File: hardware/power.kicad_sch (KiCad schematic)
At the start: 80 parts, among them Q1 BSN20, Q2 AO3415A, U3 SY8088, U4 SY8088, U5 SY8088, U6 SY8089A, U7 SY8113, U8 SY8088

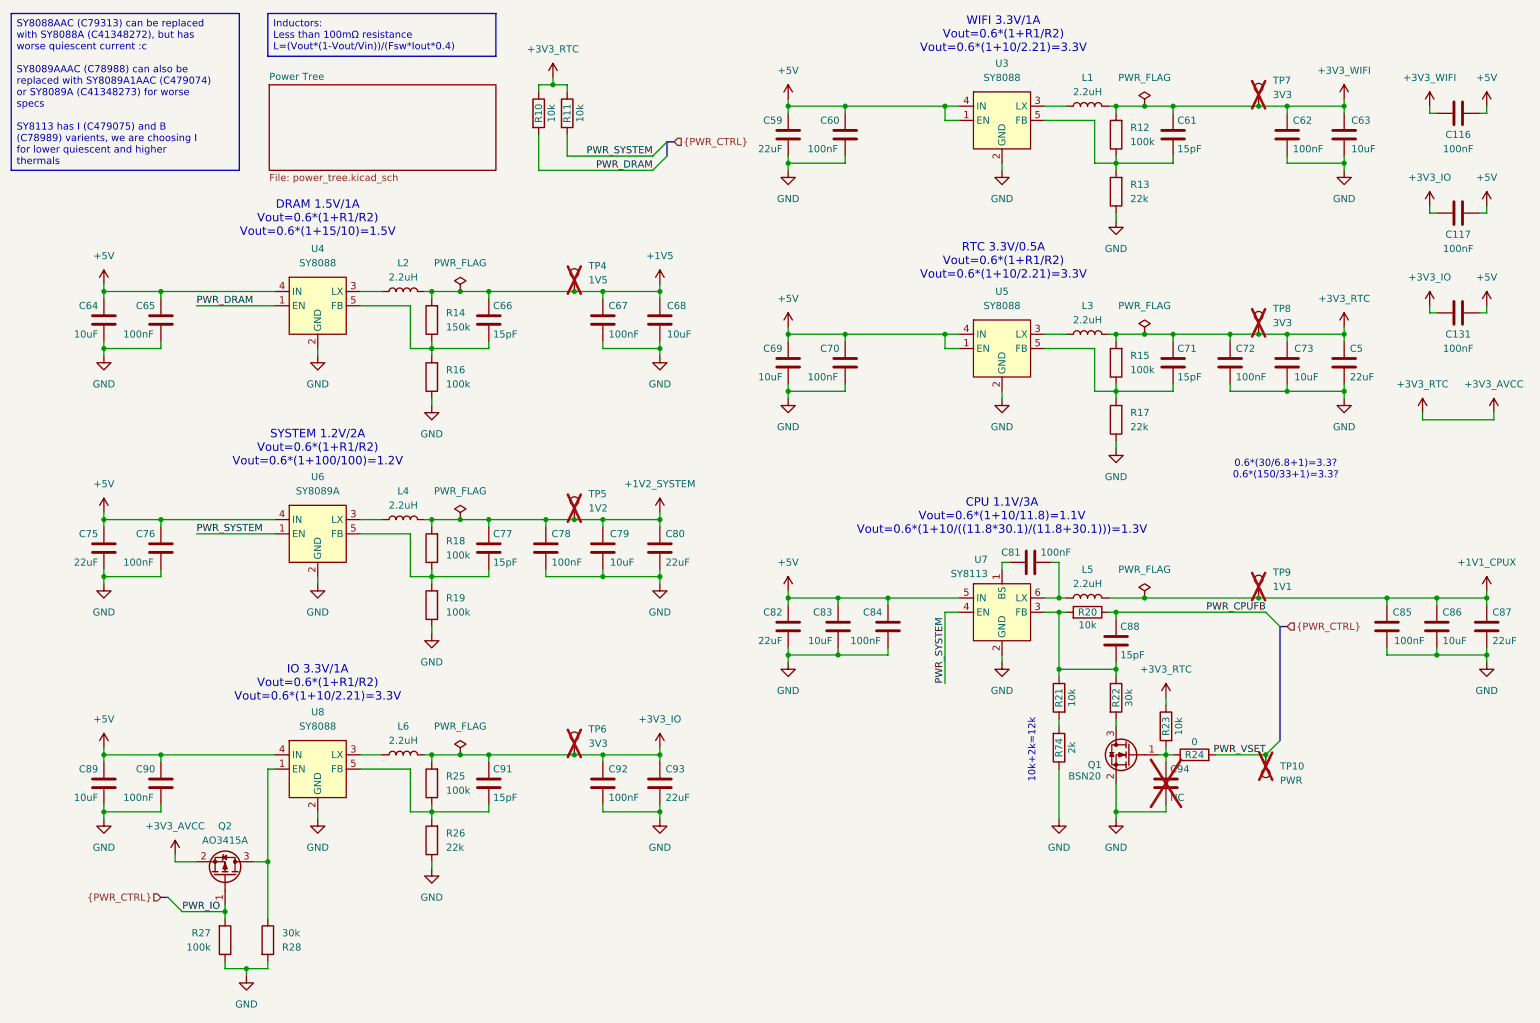
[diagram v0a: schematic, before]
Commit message: Update crystal
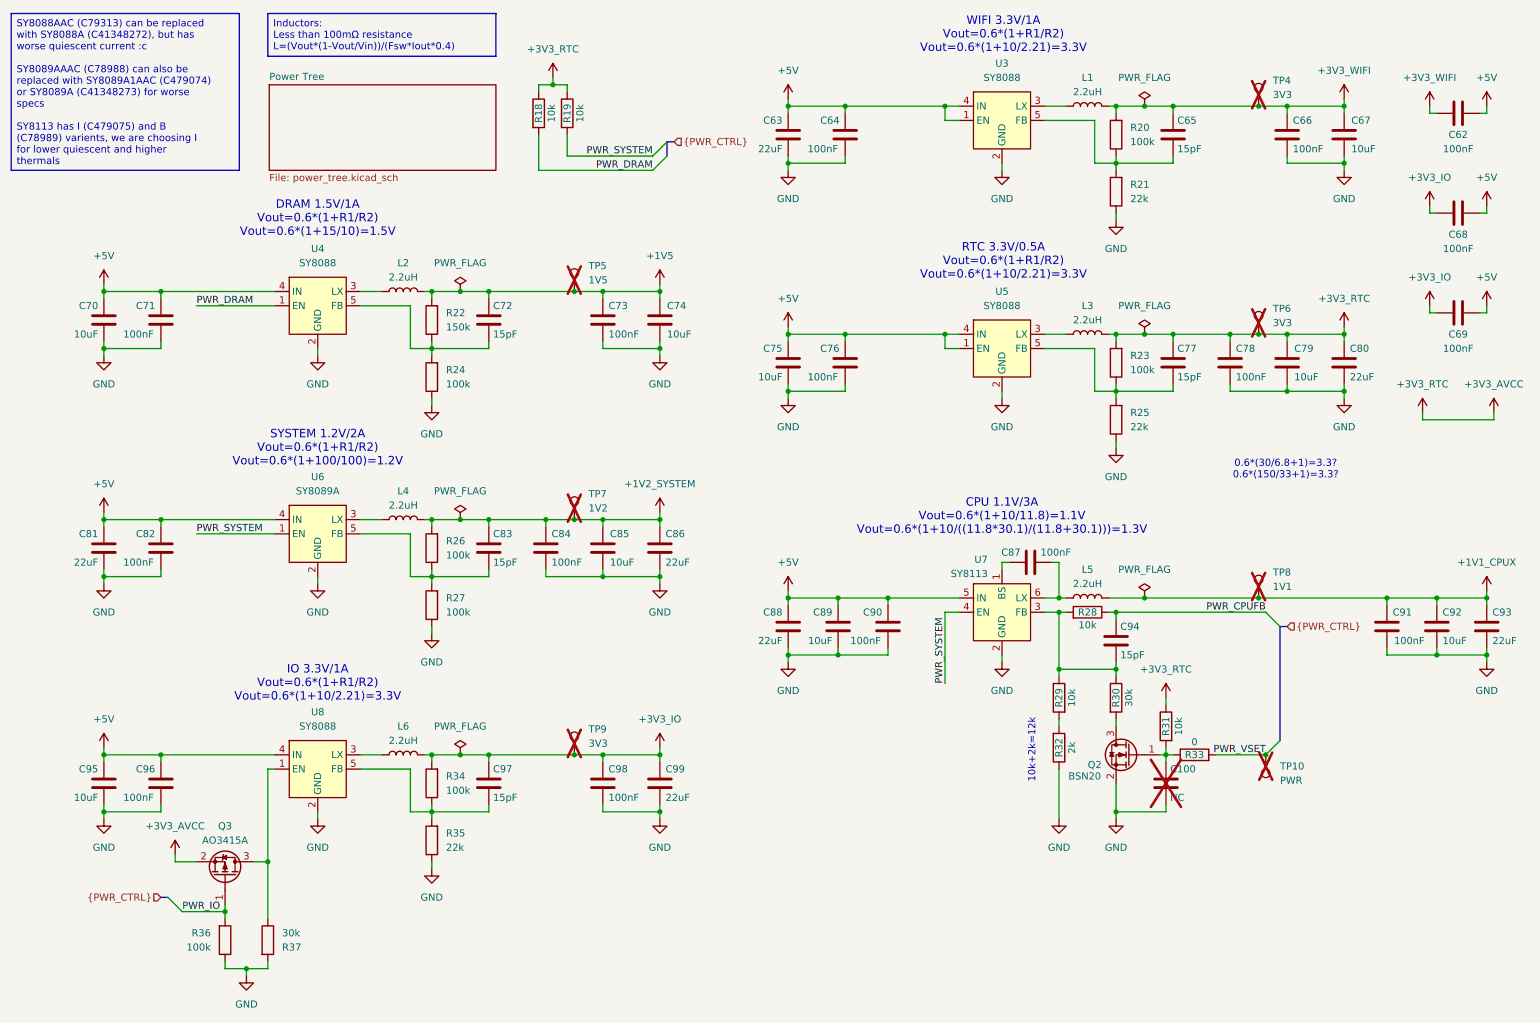
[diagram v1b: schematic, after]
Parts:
- renumbered C94 to C100, C116 to C62, C59 to C63, C60 to C64, C61 to C65, C62 to C66, C63 to C67, C117 to C68, C131 to C69, C64 to C70, C65 to C71, C66 to C72, C67 to C73, C68 to C74, C69 to C75, C70 to C76, C71 to C77, C72 to C78, C73 to C79, C5 to C80, C75 to C81, C76 to C82, C77 to C83, C78 to C84, C79 to C85, C80 to C86, C81 to C87, C82 to C88, C83 to C89, C84 to C90, C85 to C91, C86 to C92, C87 to C93, C88 to C94, C89 to C95, C90 to C96, C91 to C97, C92 to C98, C93 to C99, Q1 to Q2, Q2 to Q3, R10 to R18, R11 to R19, R12 to R20, R13 to R21, R14 to R22, R15 to R23, R16 to R24, R17 to R25, R18 to R26, R19 to R27, R20 to R28, R21 to R29, R22 to R30, R23 to R31, R74 to R32, R24 to R33, R25 to R34, R26 to R35, R27 to R36, R28 to R37, TP7 to TP4, TP4 to TP5, TP8 to TP6, TP5 to TP7, TP9 to TP8, TP6 to TP9

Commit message: Add schematic pdf
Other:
- title: Icepi CM0 -> Icepi SBC
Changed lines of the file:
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@@
 	(paper "A4")
 	(title_block
-		(title "Icepi CM0")
-		(date "2025-11-21")
+		(title "Icepi SBC")
+		(date "2025-12-21")
 		(rev "v1.0")
 		(company "Icy Electronics")
 		(comment 1 "Chengyin Yao (cheyao)")
-		(comment 2 "https://github.com/cheyao/icepi-cm0")
+		(comment 2 "https://github.com/cheyao/icepi-sbc")
 		(comment 3 "License: Solderpad")
 	)
